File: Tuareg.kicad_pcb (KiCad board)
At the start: 4 copper layers, 101.6 x 103.6 mm, 202 parts, among them CON1 ModICE_48, J1 SWD_boctok, P1 VNLD5090e, P2 FAN1100, P3 VNLD5090e, P4 FAN1100, P5 ISO7421D, Q1 BTS3028SDL, Q2 BTS3028SDL, Q3 ISL9V3040, Q4 BTS3028SDL, Q5 ISL9V3040, U1 NCV1117DT, U2 NCV1117ST, U3 MCP6004, U4 MCP6004, U5 LM2903, U6 STM32F410RBTx, U7 24C64, Y1 lfxtal071673, Y2 cx5032ga

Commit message: cleaning up bottom layer
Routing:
- net GND: track 509.4 -> 471.1 mm
- net /crash: track 83.1 -> 84.2 mm
- net /con_vcci: track 23.2 -> 22.4 mm
- net +3V3: track 213.0 -> 212.3 mm

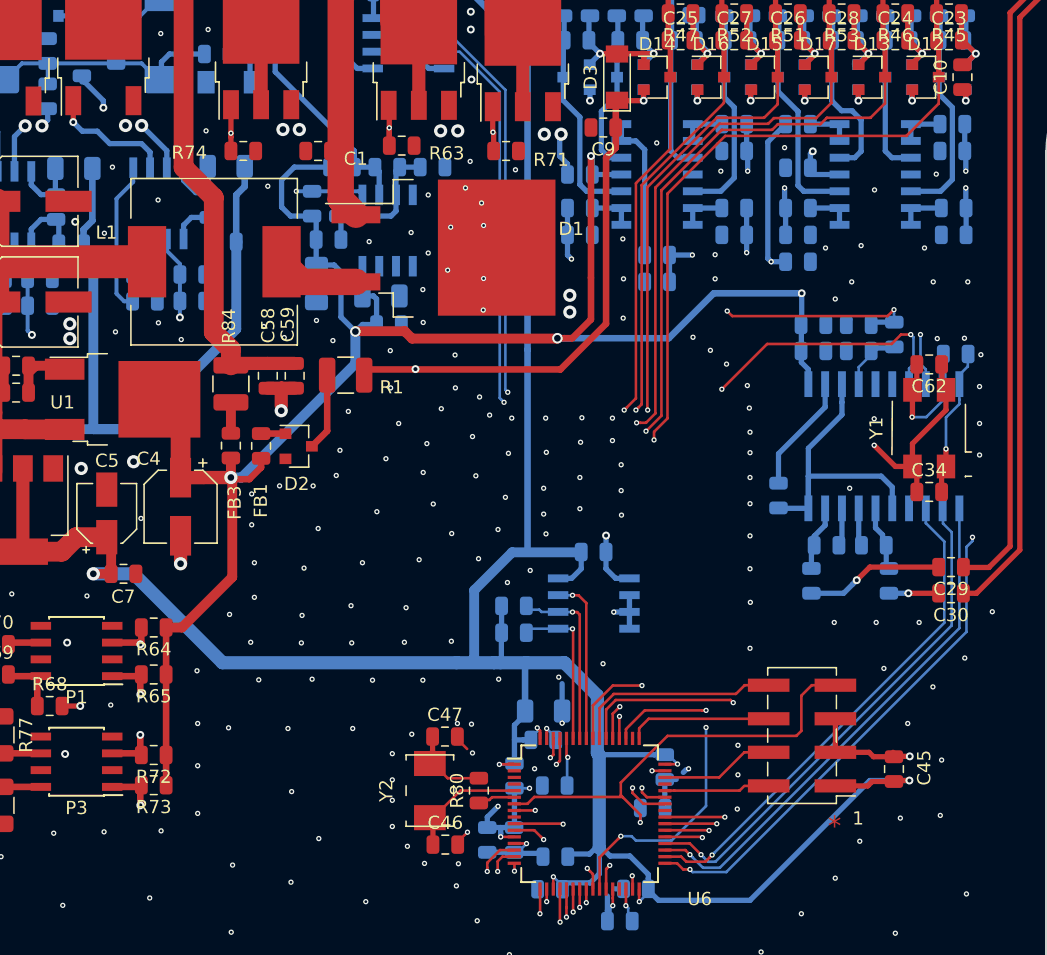
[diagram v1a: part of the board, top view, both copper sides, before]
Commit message: cleaning up fab layers
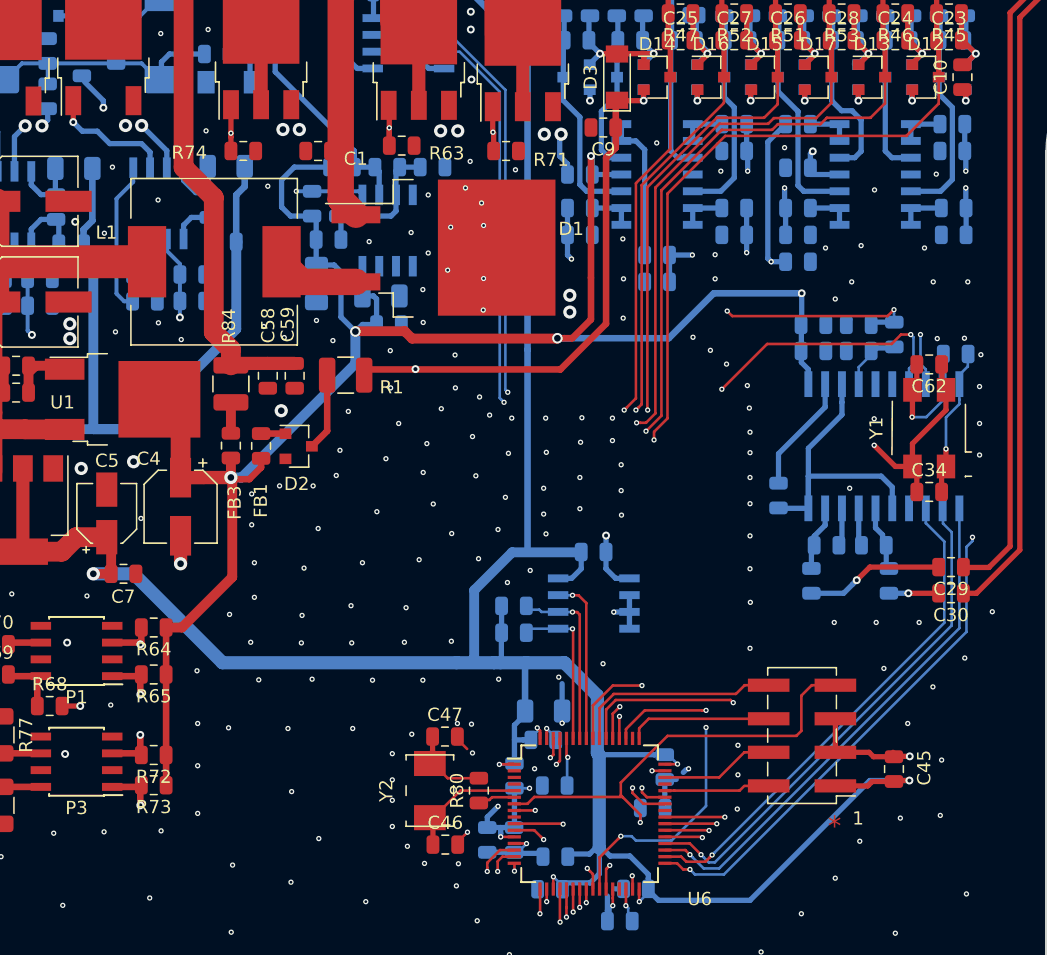
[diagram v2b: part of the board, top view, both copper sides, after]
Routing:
- net GND: track 471.1 -> 467.7 mm
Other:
- board text added: "SWD"

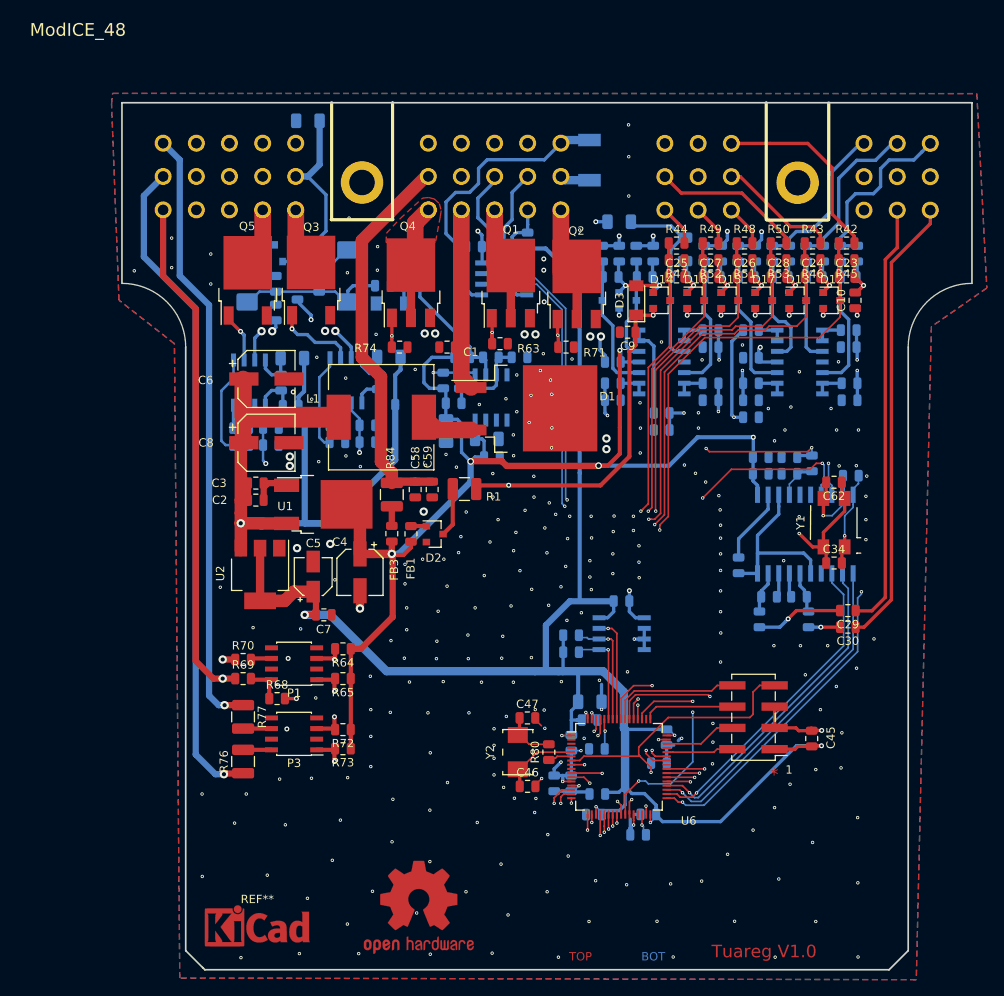
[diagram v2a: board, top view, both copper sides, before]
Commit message: added aisler design rules, cleaning up
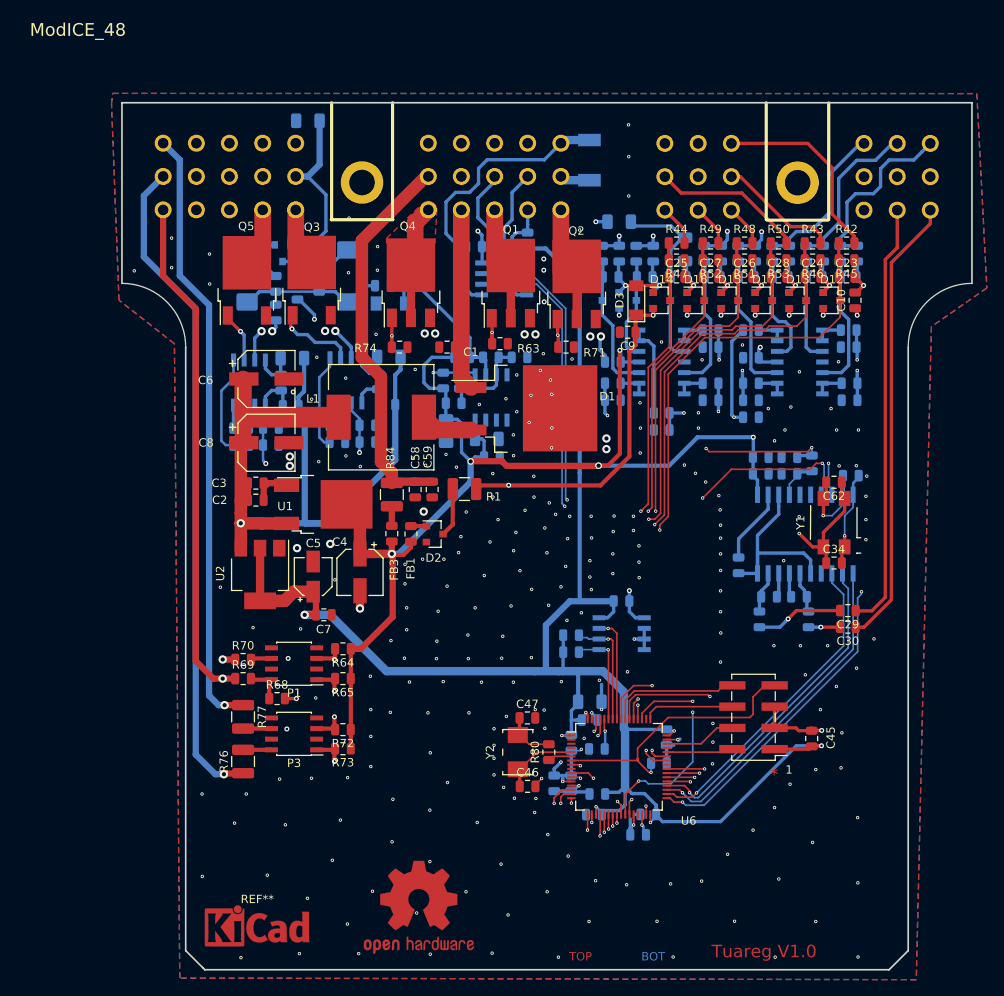
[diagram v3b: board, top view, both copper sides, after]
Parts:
- moved Q5 0.10 mm to (92.7, 73.0)
- moved Q3 0.08 mm to (100.4, 73.0)
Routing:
- net /crash: track 84.2 -> 82.9 mm
- net Net-(C65-Pad1): track 9.04 -> 8.26 mm
- net Net-(C21-Pad1): track 20.2 -> 19.4 mm
- net GND: track 467.7 -> 467.0 mm, vias 283 -> 282
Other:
- net class uc: clearance 0.1 -> 0.2
- net class ultra: clearance 0.8 -> 0.9
- net class vr: clearance 0.1 -> 0.2

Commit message: cleaning up
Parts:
- moved R34 2.82 mm to (102.6, 54.9), turned to 0 degrees
- moved C44 1.39 mm to (136.0, 111.4)
- moved C64 1.12 mm to (116.5, 89.9), turned to 180 degrees
- moved C63 0.48 mm to (122.4, 94.2)
- moved C22 0.08 mm to (121.3, 92.0)
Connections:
- CON1 pad 13: /con_ach4 -> GND
- CON1 pad 34: /con_vrcrank+ -> GND
- CON1 pad 37: GND -> /con_spareact2
- CON1 pad 44: GND -> /con_vrcrank+
- CON1 pad 48: /con_spareact2 -> GND
- CON1 pad 8: GND -> /con_ach4
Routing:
- net GND: track 467.0 -> 477.4 mm, vias 282 -> 278
- net /con_ach8: track 41.1 -> 33.3 mm
- net +12V: track 203.7 -> 196.5 mm
- net /con_ach4: track 21.7 -> 15.1 mm
- net /con_spareact2: track 72.8 -> 68.8 mm
- net +5V: track 183.6 -> 180.8 mm
- net +3V3: track 212.4 -> 209.8 mm
- net /INJ2: track 72.7 -> 74.2 mm
- net /con_ach2: track 19.2 -> 19.8 mm
- net Net-(P4-Pad5): track 11.9 -> 11.4 mm

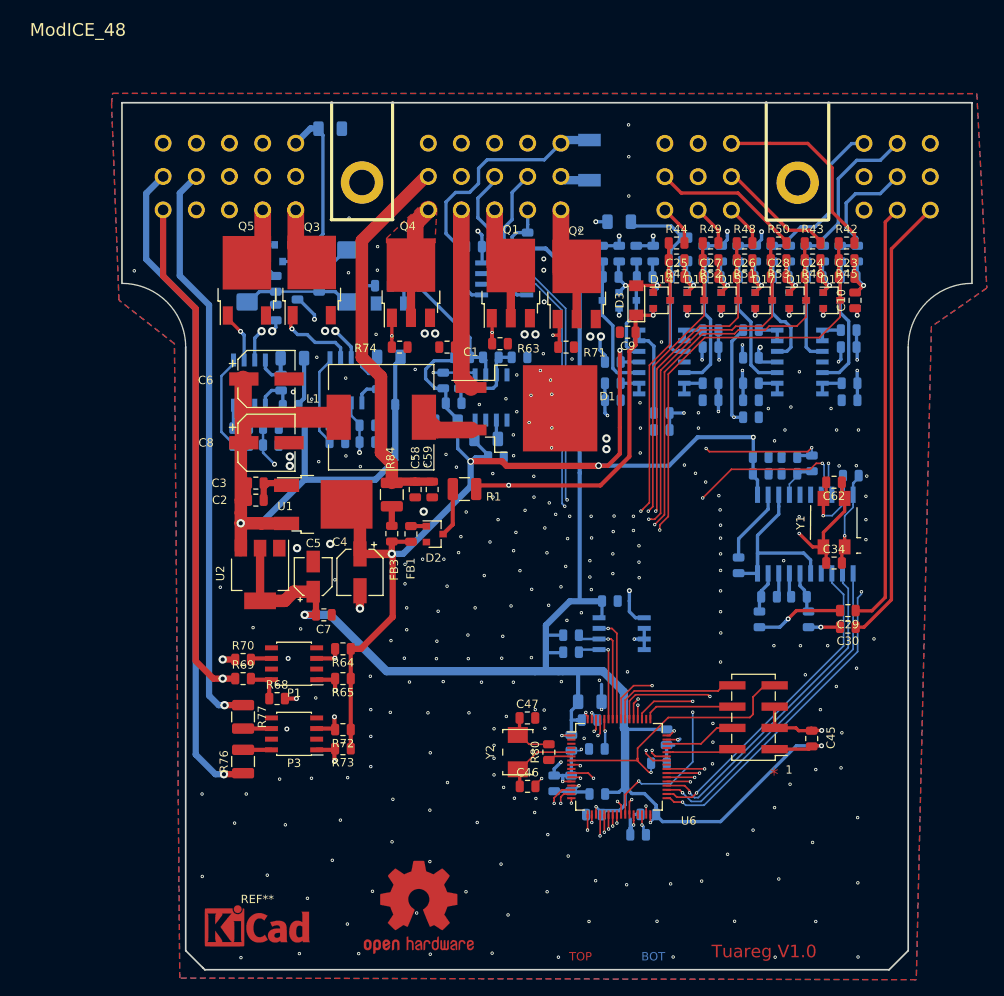
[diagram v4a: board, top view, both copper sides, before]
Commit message: added test points and cleaning up silk screen
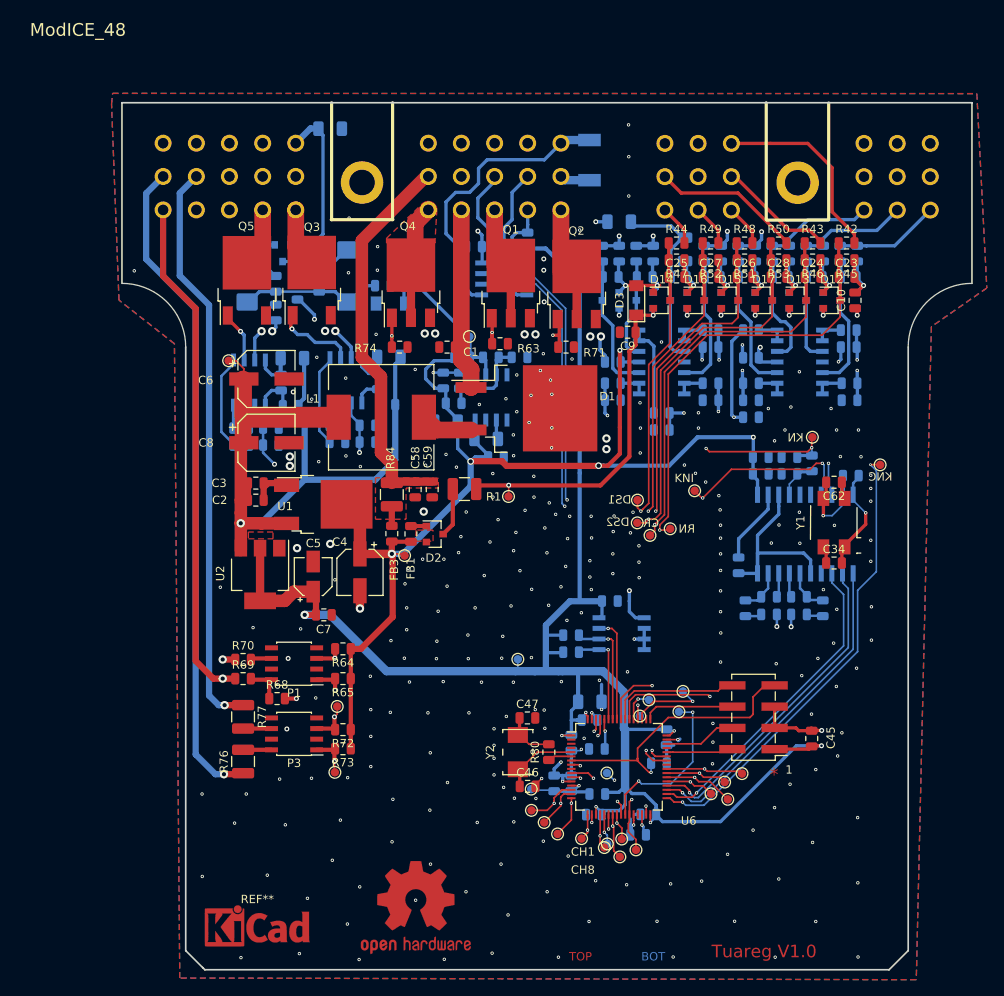
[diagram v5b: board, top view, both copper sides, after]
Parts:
- added 12V: TestPoint_Pad_D1.0mm, TestPoint:TestPoint_Pad_D1.0mm, F.Cu at (90.5, 82.7)
- added 33V: TestPoint_Pad_D1.0mm, TestPoint:TestPoint_Pad_D1.0mm, F.Cu at (125.0, 118.3)
- added 5V: TestPoint_Pad_D1.0mm, TestPoint:TestPoint_Pad_D1.0mm, F.Cu at (111.5, 105.9)
- added 5VC: TestPoint_Pad_D1.0mm, TestPoint:TestPoint_Pad_D1.0mm, F.Cu at (123.9, 98.9)
- added BAT: TestPoint_Pad_D1.0mm, TestPoint:TestPoint_Pad_D1.0mm, F.Cu at (135.7, 140.4)
- added CH1: TestPoint_Pad_D1.0mm, TestPoint:TestPoint_Pad_D1.0mm, F.Cu at (132.7, 139.8)
- added CH2: TestPoint_Pad_D1.0mm, TestPoint:TestPoint_Pad_D1.0mm, F.Cu at (129.8, 139.2)
- added CH3: TestPoint_Pad_D1.0mm, TestPoint:TestPoint_Pad_D1.0mm, F.Cu at (128.2, 137.8)
- added CH4: TestPoint_Pad_D1.0mm, TestPoint:TestPoint_Pad_D1.0mm, F.Cu at (126.7, 136.4)
- added CH5: TestPoint_Pad_D1.0mm, TestPoint:TestPoint_Pad_D1.0mm, F.Cu at (137.5, 139.8)
- added CH6: TestPoint_Pad_D1.0mm, TestPoint:TestPoint_Pad_D1.0mm, F.Cu at (137.2, 142.0)
- added CH8: TestPoint_Pad_D1.0mm, TestPoint:TestPoint_Pad_D1.0mm, F.Cu at (135.4, 140.8)
- added CO1: TestPoint_Pad_D1.0mm, TestPoint:TestPoint_Pad_D1.0mm, F.Cu at (148.1, 134.4)
- added CO2: TestPoint_Pad_D1.0mm, TestPoint:TestPoint_Pad_D1.0mm, F.Cu at (150.1, 135.1)
- added CR: TestPoint_Pad_D1.0mm, TestPoint:TestPoint_Pad_D1.0mm, F.Cu at (140.8, 103.5)
- added CRK: TestPoint_Pad_D1.0mm, TestPoint:TestPoint_Pad_D1.0mm, F.Cu at (144.3, 124.6)
- added DBG: TestPoint_Pad_D1.0mm, TestPoint:TestPoint_Pad_D1.0mm, F.Cu at (135.7, 131.9)
- added DS1: TestPoint_Pad_D1.0mm, TestPoint:TestPoint_Pad_D1.0mm, F.Cu at (139.3, 99.3)
- added DS2: TestPoint_Pad_D1.0mm, TestPoint:TestPoint_Pad_D1.0mm, F.Cu at (139.3, 102.0)
- added FUP: TestPoint_Pad_D1.0mm, TestPoint:TestPoint_Pad_D1.0mm, F.Cu at (144.8, 122.2)
- added IJ1: TestPoint_Pad_D1.0mm, TestPoint:TestPoint_Pad_D1.0mm, F.Cu at (149.8, 133.0)
- added IJ2: TestPoint_Pad_D1.0mm, TestPoint:TestPoint_Pad_D1.0mm, F.Cu at (151.8, 132.0)
- added KN: TestPoint_Pad_D1.0mm, TestPoint:TestPoint_Pad_D1.0mm, F.Cu at (160.2, 91.8)
- added KNC: TestPoint_Pad_D1.0mm, TestPoint:TestPoint_Pad_D1.0mm, F.Cu at (168.4, 95.1)
- added KNI: TestPoint_Pad_D1.0mm, TestPoint:TestPoint_Pad_D1.0mm, F.Cu at (146.2, 98.2)
- added LA: TestPoint_Pad_D1.0mm, TestPoint:TestPoint_Pad_D1.0mm, F.Cu at (140.7, 123.2)
- added RN: TestPoint_Pad_D1.0mm, TestPoint:TestPoint_Pad_D1.0mm, F.Cu at (143.3, 102.7)
- added SA1: TestPoint_Pad_D1.0mm, TestPoint:TestPoint_Pad_D1.0mm, F.Cu at (103.2, 131.9)
- added SA2: TestPoint_Pad_D1.0mm, TestPoint:TestPoint_Pad_D1.0mm, F.Cu at (103.5, 124.0)
- added TA: TestPoint_Pad_D1.0mm, TestPoint:TestPoint_Pad_D1.0mm, F.Cu at (139.6, 125.1)
- added VDDA: TestPoint_Pad_D1.0mm, TestPoint:TestPoint_Pad_D1.0mm, F.Cu at (126.6, 133.9)
- added VR: TestPoint_Pad_D1.0mm, TestPoint:TestPoint_Pad_D1.0mm, F.Cu at (119.3, 79.8)
- added cam: TestPoint_Pad_D1.0mm, TestPoint:TestPoint_Pad_D1.0mm, F.Cu at (139.2, 141.1)
- C29, C30: moved to B.Cu
- moved C29 9.43 mm to (155.1, 113.0)
- moved C30 6.04 mm to (158.6, 113.0), turned to 0 degrees
- moved R55 2.15 mm to (161.5, 112.2)
- moved R54 2.13 mm to (152.2, 112.2)
- moved REF** 0.36 mm to (112.9, 148.0)
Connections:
- CON1 pad 1: /con_knock2 -> /con_ach4
- CON1 pad 14: /con_ach3 -> GND
- CON1 pad 15: /con_ach2 -> /con_ach1
- CON1 pad 2: /con_knock1 -> /con_ach3
- CON1 pad 3: GND -> /con_ach2
- CON1 pad 7: /con_ach8 -> /con_knock2
- CON1 pad 8: /con_ach4 -> /con_knock1
- CON1 pad 9: /con_ach1 -> /con_ach8
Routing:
- net GND: track 477.4 -> 448.7 mm, vias 278 -> 284
- net /con_knock1: track 51.2 -> 62.8 mm, vias 0 -> 1
- net /con_knock2: track 54.1 -> 63.8 mm, vias 0 -> 1
- net Net-(C29-Pad2): track 10.4 -> 1.97 mm, vias 1 -> 0
- net /con_ach2: track 19.8 -> 13.2 mm
- net /con_ach3: track 19.6 -> 13.1 mm
- net /knock_cs: track 59.0 -> 64.5 mm
- net /COIL2: track 97.6 -> 102.6 mm
- net /INJ2: track 74.2 -> 78.9 mm
- net /cam: track 78.1 -> 82.8 mm
- net /ach2: track 88.2 -> 92.8 mm
- net /ach6: track 69.9 -> 73.9 mm
- net /con_ach1: track 19.0 -> 22.8 mm
- net +12V: track 196.5 -> 200.0 mm
- net /INJ1: track 80.2 -> 83.6 mm
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
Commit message: corrected silk screen and fab layers
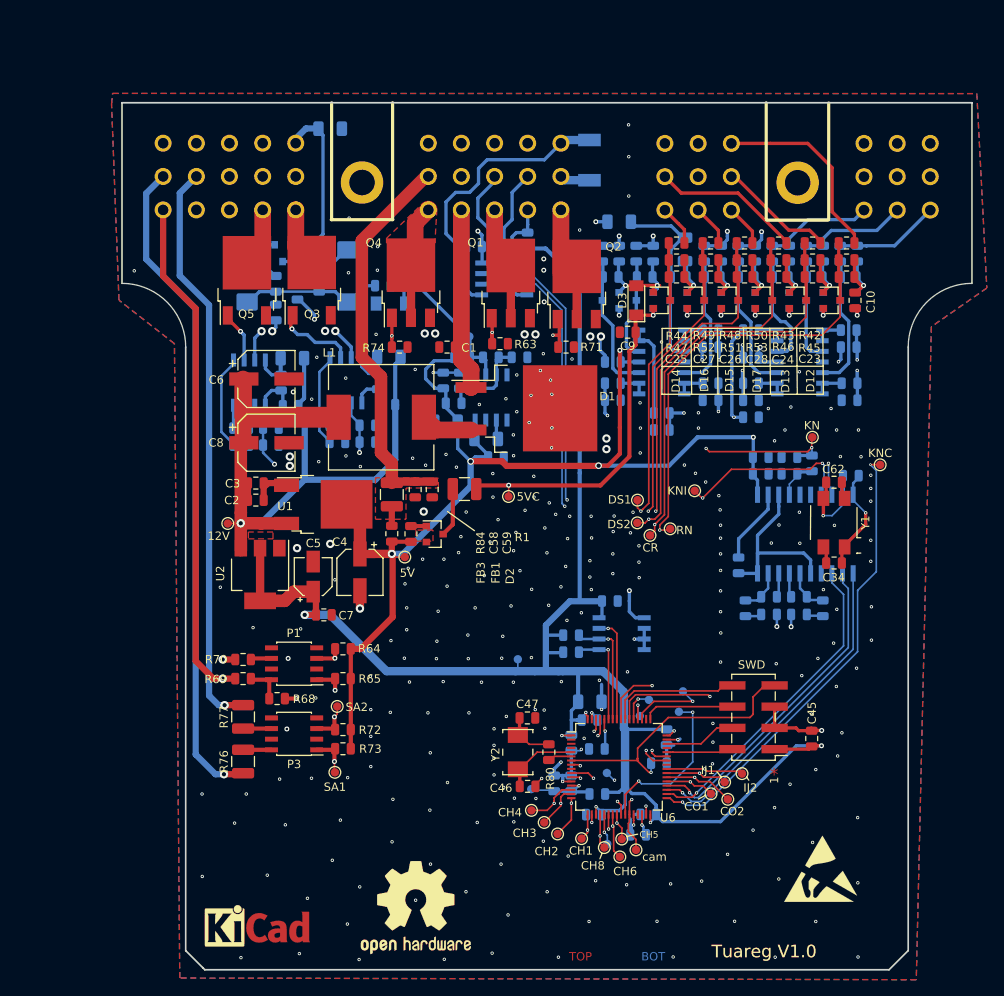
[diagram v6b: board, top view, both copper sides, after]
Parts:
- added REF**: ESD-Logo_8.9x8mm_SilkScreen, Symbol:ESD-Logo_8.9x8mm_SilkScreen, F.Cu at (161.2, 143.4)
- 33V, BAT, CRK, DBG, FUP, LA, TA, VDDA, VR: moved to B.Cu
- moved 12V 19.5 mm to (90.4, 102.1)
- moved 5V 0.18 mm to (111.5, 106.1)
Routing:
- net +12V: track 200.0 -> 198.1 mm
